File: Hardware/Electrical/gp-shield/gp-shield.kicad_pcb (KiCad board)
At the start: 2 copper layers, 72.4 x 53.3 mm, 210 parts, among them J1 XT60/TERM2, J10 Conn_01x08, J11 Conn_01x04, J12 Conn_01x08, J13 T821-02x08, J14 Conn_01x04, J15 Conn_01x07, J2 XT60/TERM2, J3 Conn_01x04, J4 Conn_01x03, J5 Conn_01x03, J6 Conn_01x03, J7 Conn_01x03, J8 Conn_01x03, J9 Conn_01x03, Q1 Q_PMOS_GDS, Q3 Q_NMOS_GDS, SW1 SW_SPDT, SW2 SW_Push, SW3 SW_Push, U1 NCP1117-5.0_SOT223, U2 LM4040DBZ-2.5, U4 LM397

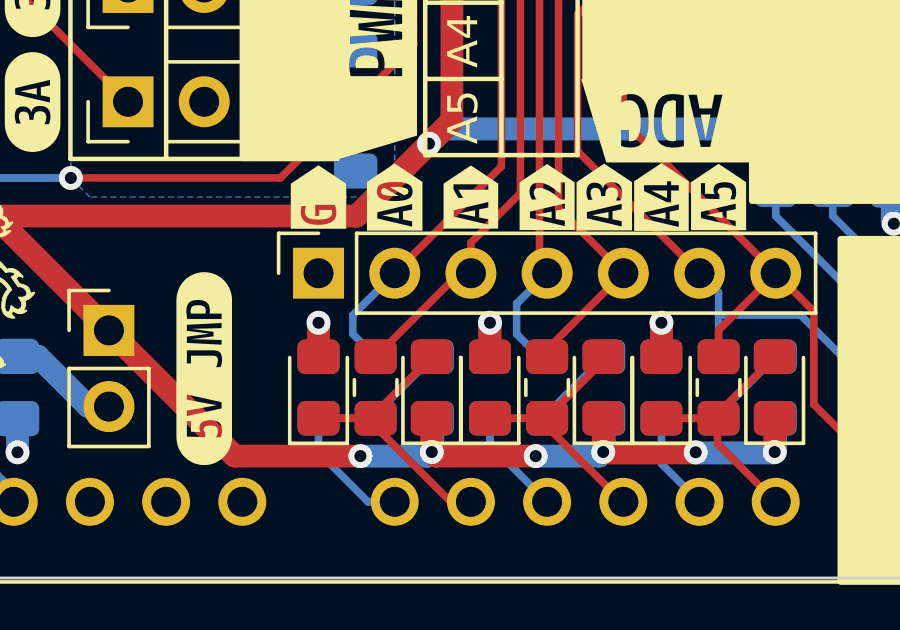
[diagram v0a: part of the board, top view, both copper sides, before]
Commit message: Minor cosmetic imporvements
title block and colour theme
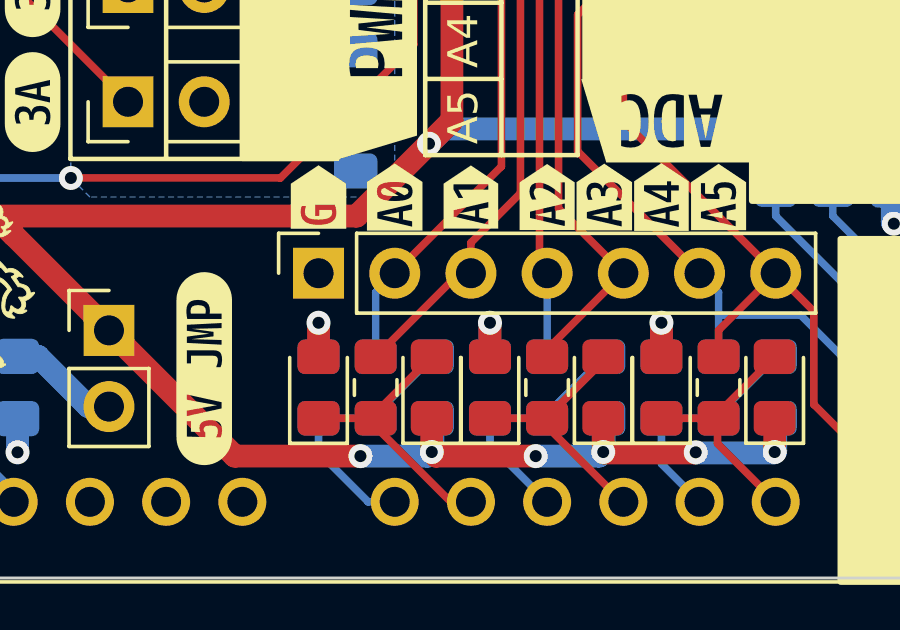
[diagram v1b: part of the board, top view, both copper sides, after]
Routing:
- net /IO/ADC.AN2: track 20.3 -> 19.3 mm
- net /IO/ADC.AN0: track 27.4 -> 26.8 mm
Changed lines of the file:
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@@
     (fp_line (start -2.54 -3.81) (end -2.54 -3.35) (layer "F.SilkS") (width 0.12))
     (fp_line (start -5.21 0) (end -5.21 6.15) (layer "F.SilkS") (width 0.12))
-    (fp_arc (start 7.62 -3.35) (mid 9.517889 -2.12363) (end 10.29 0) (layer "F.SilkS") (width 0.12))
+    (fp_arc (start 7.62 -3.35) (mid 9.51789 -2.123631) (end 10.29 0) (layer "F.SilkS") (width 0.12))
     (fp_arc (start -5.21 0) (mid -4.437886 -2.123629) (end -2.54 -3.35) (layer "F.SilkS") (width 0.12))
     (fp_line (start -2.71 -4) (end -2.71 -3.502) (layer "F.CrtYd") (width 0.05))
@@
     (fp_line (start -5.331 -0.073) (end -5.331 6.277) (layer "F.CrtYd") (width 0.05))
     (fp_line (start 10.417 6.277) (end -5.331 6.277) (layer "F.CrtYd") (width 0.05))
-    (fp_arc (start 7.79 -3.502) (mid 9.691343 -2.237853) (end 10.417 -0.073) (layer "F.CrtYd") (width 0.05))
+    (fp_arc (start 7.79 -3.502) (mid 9.69134 -2.237853) (end 10.417 -0.073) (layer "F.CrtYd") (width 0.05))
     (fp_arc (start -5.331 -0.073) (mid -4.608341 -2.236824) (end -2.71 -3.502) (layer "F.CrtYd") (width 0.05))
     (fp_line (start -2.41 2.55) (end 7.49 2.55) (layer "F.Fab") (width 0.1))
@@
     (fp_line (start -2.54 -3.81) (end -2.54 -3.35) (layer "F.SilkS") (width 0.12))
     (fp_line (start -2.54 0.635) (end -2.54 3.81) (layer "F.SilkS") (width 0.12))
-    (fp_arc (start 7.62 -3.35) (mid 9.517889 -2.12363) (end 10.29 0) (layer "F.SilkS") (width 0.12))
+    (fp_arc (start 7.62 -3.35) (mid 9.51789 -2.123631) (end 10.29 0) (layer "F.SilkS") (width 0.12))
     (fp_arc (start -5.21 0) (mid -4.437886 -2.123629) (end -2.54 -3.35) (layer "F.SilkS") (width 0.12))
     (fp_line (start 10.417 6.277) (end -5.331 6.277) (layer "F.CrtYd") (width 0.05))
@@
     (fp_line (start -2.71 -4) (end -2.71 -3.502) (layer "F.CrtYd") (width 0.05))
     (fp_line (start -2.71 -4) (end 7.79 -4) (layer "F.CrtYd") (width 0.05))
-    (fp_arc (start 7.79 -3.502) (mid 9.691343 -2.237853) (end 10.417 -0.073) (layer "F.CrtYd") (width 0.05))
+    (fp_arc (start 7.79 -3.502) (mid 9.69134 -2.237853) (end 10.417 -0.073) (layer "F.CrtYd") (width 0.05))
     (fp_arc (start -5.331 -0.073) (mid -4.608341 -2.236824) (end -2.71 -3.502) (layer "F.CrtYd") (width 0.05))
     (fp_line (start -2.46 3.75) (end 7.54 3.75) (layer "F.Fab") (width 0.1))
@@
   (segment (start 141.351 91.059) (end 137.795 94.615) (width 0.254) (layer "F.Cu") (net 54))
   (segment (start 141.351 78.3765) (end 141.351 91.059) (width 0.254) (layer "F.Cu") (net 54))
+  (segment (start 137.16 95.25) (end 137.795 94.615) (width 0.25) (layer "B.Cu") (net 54))
+  (segment (start 137.16 97.4) (end 137.16 95.25) (width 0.25) (layer "B.Cu") (net 54))
   (segment (start 137.16 97.4) (end 137.16 97.155) (width 0.254) (layer "B.Cu") (net 54))
-  (segment (start 137.16 97.4) (end 136.398 96.638) (width 0.25) (layer "B.Cu") (net 54))
-  (segment (start 136.398 96.638) (end 136.398 96.012) (width 0.25) (layer "B.Cu") (net 54))
-  (segment (start 136.398 96.012) (end 137.795 94.615) (width 0.25) (layer "B.Cu") (net 54))
   (segment (start 141.986 91.948) (end 141.986 80.2815) (width 0.254) (layer "F.Cu") (net 55))
   (segment (start 139.945 94.615) (end 140.335 94.615) (width 0.25) (layer "F.Cu") (net 55))
@@
   (segment (start 142.621 82.1865) (end 145.4325 79.375) (width 0.254) (layer "F.Cu") (net 56))
   (segment (start 142.875 94.615) (end 142.621 94.361) (width 0.254) (layer "F.Cu") (net 56))
-  (segment (start 141.859 95.631) (end 141.859 96.647) (width 0.254) (layer "B.Cu") (net 56))
-  (segment (start 141.859 96.647) (end 142.612 97.4) (width 0.254) (layer "B.Cu") (net 56))
-  (segment (start 142.612 97.4) (end 142.875 97.4) (width 0.254) (layer "B.Cu") (net 56))
-  (segment (start 142.875 94.615) (end 141.859 95.631) (width 0.254) (layer "B.Cu") (net 56))
+  (segment (start 142.875 94.615) (end 142.875 97.4) (width 0.254) (layer "B.Cu") (net 56))
   (segment (start 143.256 84.0915) (end 143.256 92.456) (width 0.254) (layer "F.Cu") (net 57))
   (segment (start 145.4325 81.915) (end 143.256 84.0915) (width 0.254) (layer "F.Cu") (net 57))

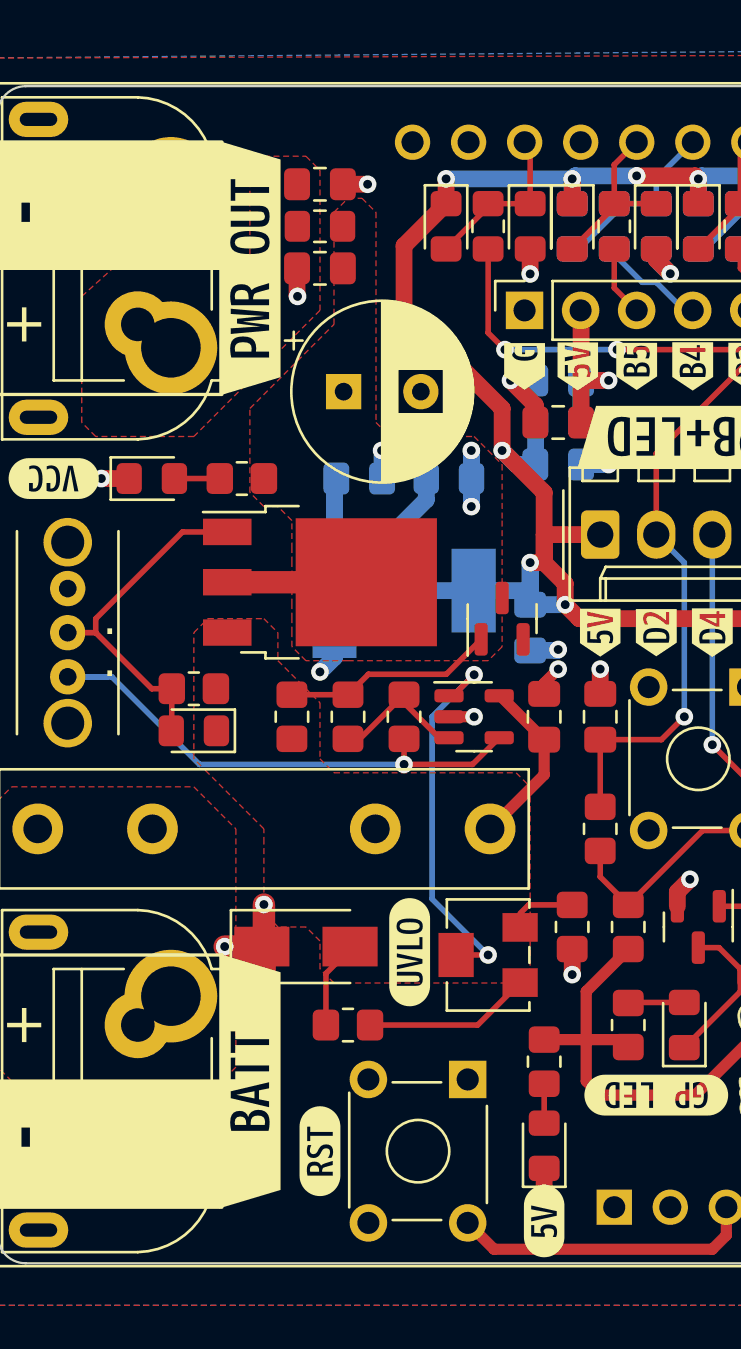
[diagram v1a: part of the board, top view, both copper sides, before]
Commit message: Added test points for key power signals
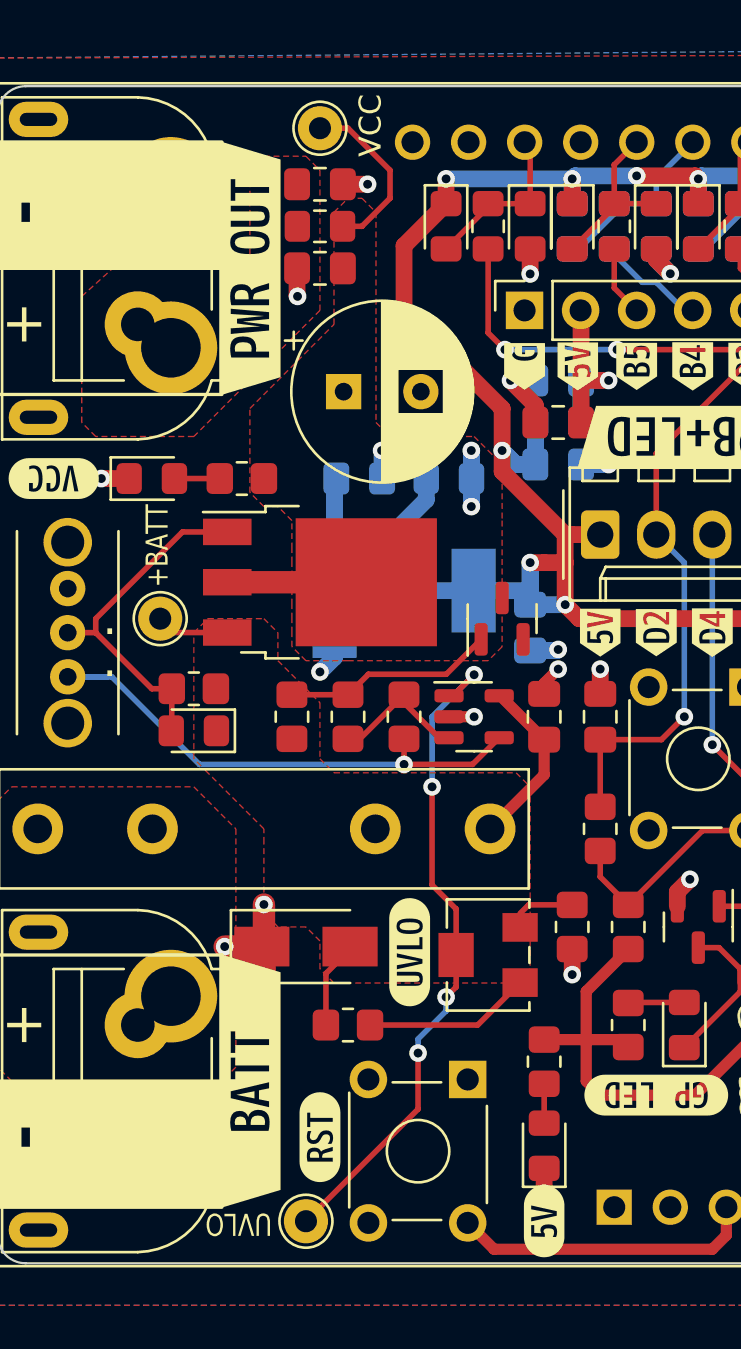
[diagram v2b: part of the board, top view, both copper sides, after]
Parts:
- added TP1: TestPoint, TestPoint:TestPoint_THTPad_D2.0mm_Drill1.0mm, F.Cu at (94.4, 75.6)
- added TP2: TestPoint, TestPoint:TestPoint_THTPad_D2.0mm_Drill1.0mm, F.Cu at (101.0, 102.9)
- added TP3: TestPoint, TestPoint:TestPoint_THTPad_D2.0mm_Drill1.0mm, F.Cu at (101.6, 53.3)
- moved kibuzzard-6352739F 0.63 mm to (101.6, 99.1)
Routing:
- net /Power/VCC_CMP-: track 18.0 -> 30.9 mm, vias 2 -> 4
- net VCC: track 9.23 -> 17.1 mm
- net /Power/+BATT_FUSED: track 12.0 -> 15.3 mm
- net +5V: track 268.0 -> 266.8 mm
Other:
- board text added: "+BATT"
- board text added: "UVLO"
- board text added: "VCC"

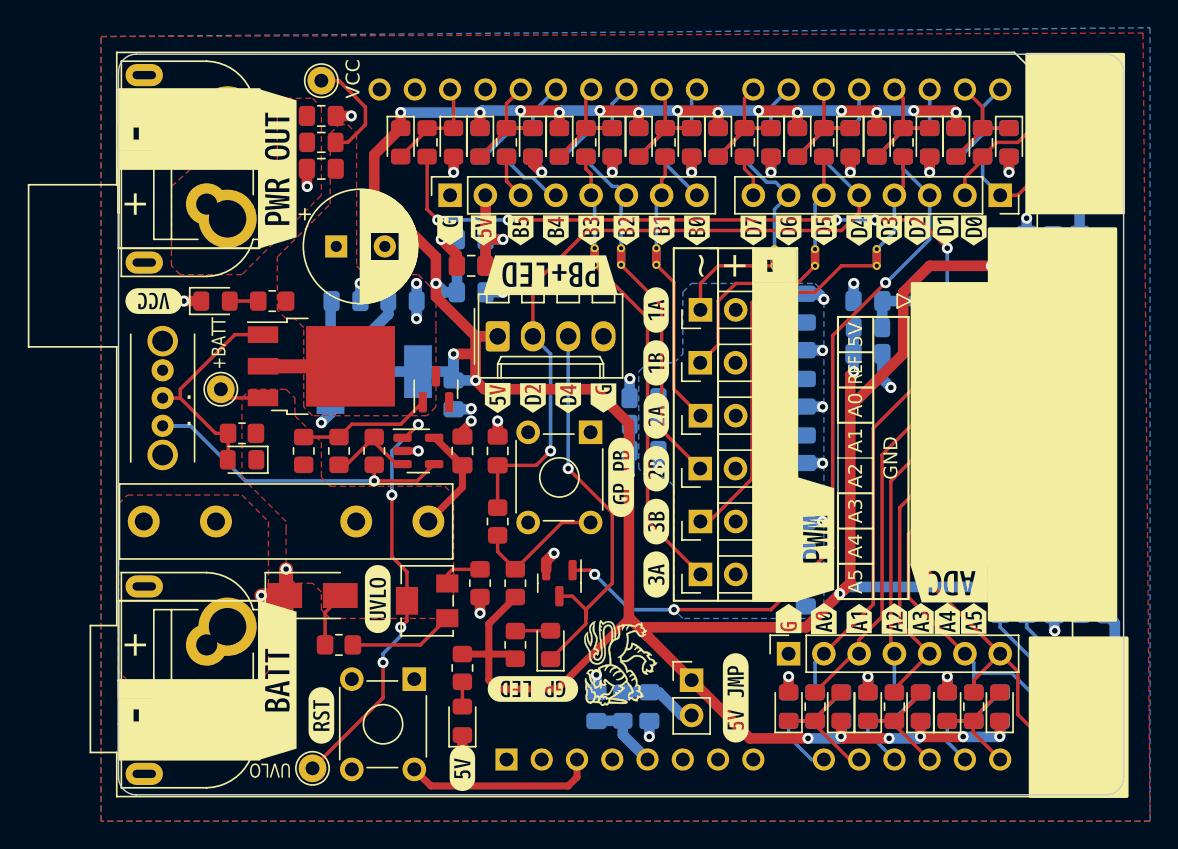
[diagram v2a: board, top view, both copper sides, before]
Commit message: Minor changes to annotation and silkscreen
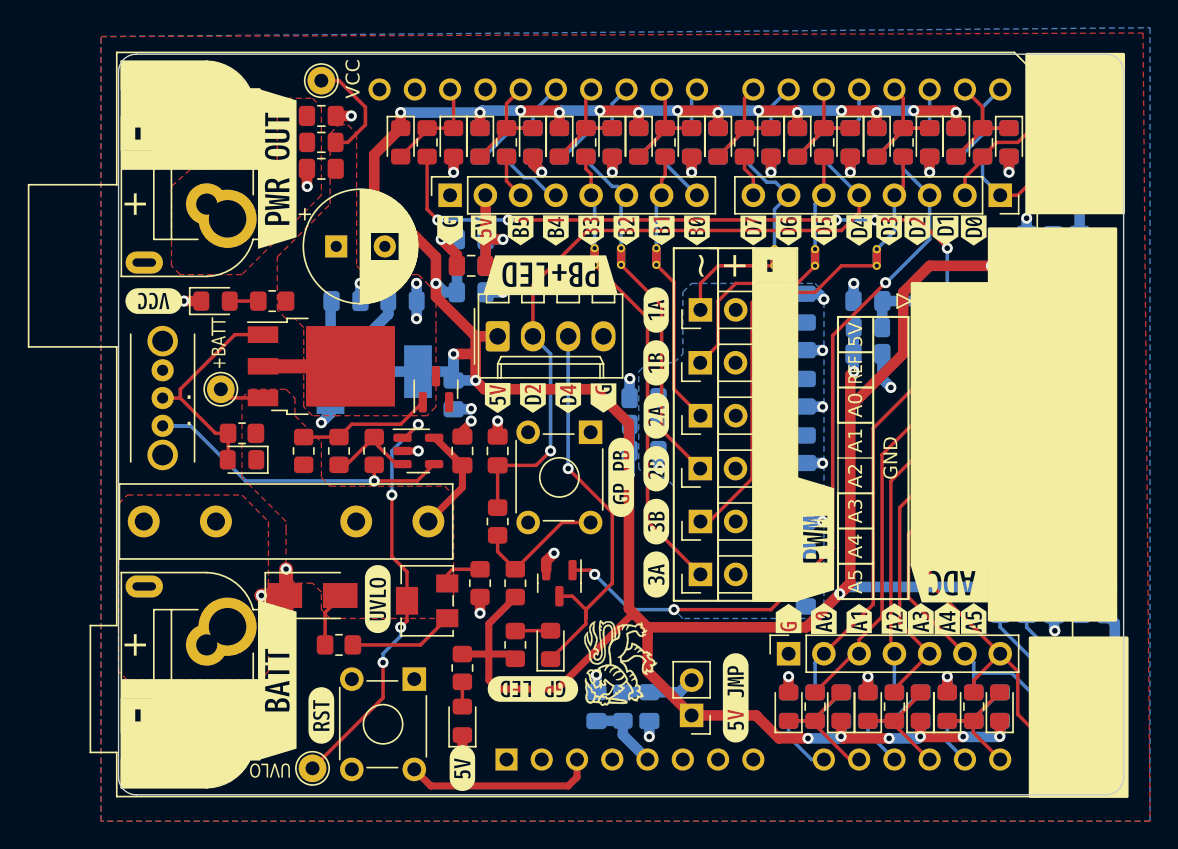
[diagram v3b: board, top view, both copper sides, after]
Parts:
- moved JP1 2.54 mm to (128.3, 99.1), turned to 180 degrees
- moved kibuzzard-636B29B0 0.13 mm to (88.4, 99.1)
- moved kibuzzard-636B29F7 0.13 mm to (88.4, 57.1)
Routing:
- net +5V: track 266.8 -> 267.5 mm
